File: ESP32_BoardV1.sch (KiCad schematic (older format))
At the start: 22 parts, among them J2 ISP, J3 To Sensor, J4 EXT. IO 1, J5 EXT. IO 1, Q1 UMH3N, U1 MIC5528-3.3YMT-TR, U2 ESP32-WROOM-32E(8MB)

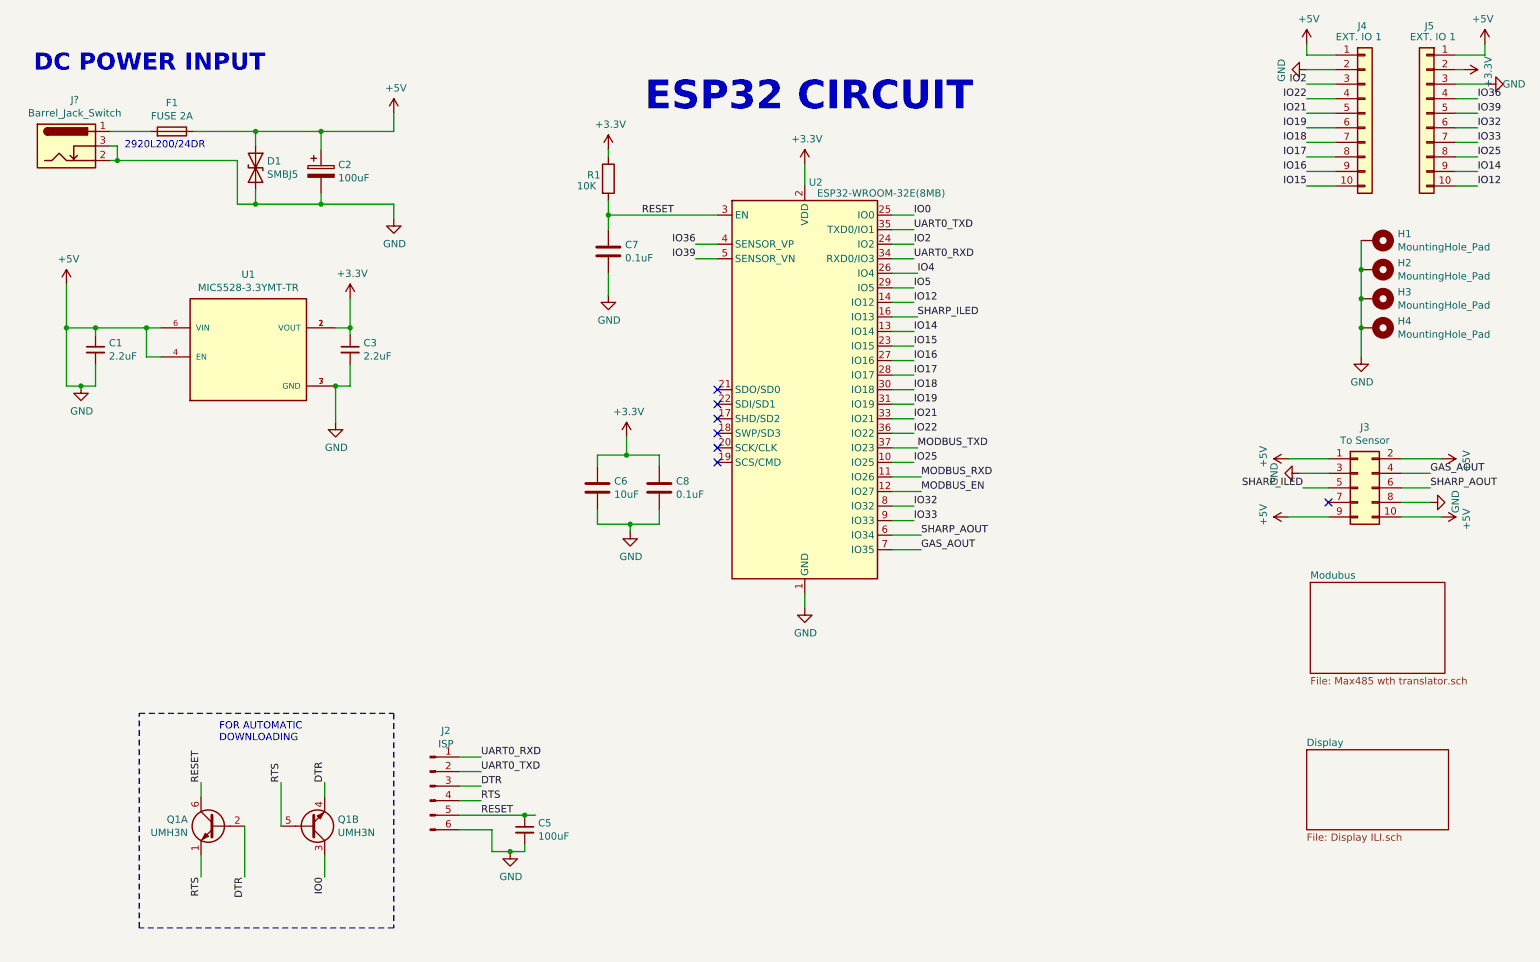
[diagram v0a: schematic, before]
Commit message: Recreated PCB file
Removed old PCB files, Schematic error in existing PCB has been rectfied
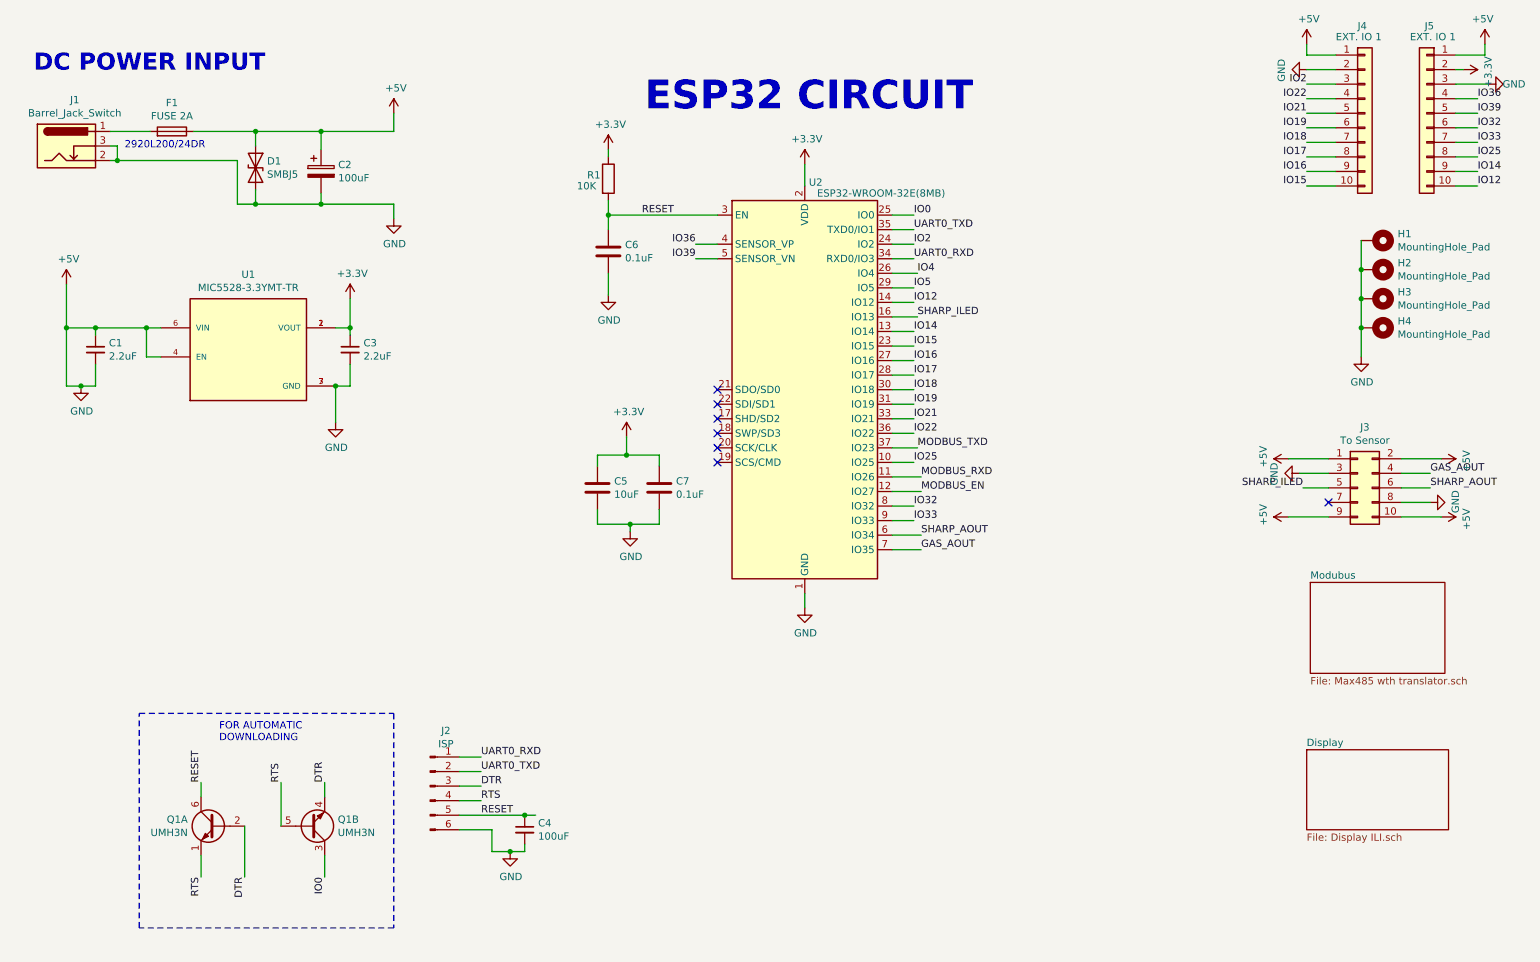
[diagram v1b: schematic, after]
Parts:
- J1: renamed from J?; footprint (none) -> Connector_BarrelJack:BarrelJack_Horizontal
- renumbered C5 to C4, C6 to C5, C7 to C6, C8 to C7
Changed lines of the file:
@@
 $Descr A4 11693 8268
 encoding utf-8
-Sheet 1 2
+Sheet 1 3
 Title ""
 Date "2020-10-15"
@@
 P 4875 2275
 AR Path="/5F7FDDC6/5F80494D" Ref="C?"  Part="1"
-AR Path="/5F80494D" Ref="C7"  Part="1"
-F 0 "C7" H 4990 2321 50  0000 L CNN
+AR Path="/5F80494D" Ref="C6"  Part="1"
+F 0 "C6" H 4990 2321 50  0000 L CNN
 F 1 "0.1uF" H 4990 2230 50  0000 L CNN
 F 2 "Capacitor_SMD:C_0805_2012Metric" H 4913 2125 50  0001 C CNN
@@
 P 5225 3900
 AR Path="/5F7FDDC6/5F80495A" Ref="C?"  Part="1"
-AR Path="/5F80495A" Ref="C8"  Part="1"
-F 0 "C8" H 5340 3946 50  0000 L CNN
+AR Path="/5F80495A" Ref="C7"  Part="1"
+F 0 "C7" H 5340 3946 50  0000 L CNN
 F 1 "0.1uF" H 5340 3855 50  0000 L CNN
 F 2 "Capacitor_SMD:C_0805_2012Metric" H 5263 3750 50  0001 C CNN
@@
 P 4800 3900
 AR Path="/5F7FDDC6/5F8049B7" Ref="C?"  Part="1"
-AR Path="/5F8049B7" Ref="C6"  Part="1"
-F 0 "C6" H 4915 3946 50  0000 L CNN
+AR Path="/5F8049B7" Ref="C5"  Part="1"
+F 0 "C5" H 4915 3946 50  0000 L CNN
 F 1 "10uF" H 4915 3855 50  0000 L CNN
 F 2 "Capacitor_SMD:C_0805_2012Metric" H 4838 3750 50  0001 C CNN
@@
 	3850 6150 4300 6150
 $Comp
-L Device:C_Small C5
+L Device:C_Small C4
 U 1 1 61CDDA04
 P 4300 6250
-F 0 "C5" H 4392 6296 50  0000 L CNN
+F 0 "C4" H 4392 6296 50  0000 L CNN
 F 1 "100uF" H 4392 6205 50  0000 L CNN
 F 2 "Capacitor_SMD:C_1206_3216Metric" H 4300 6250 50  0001 C CNN
@@
 	7000 2425 6825 2425
 $Comp
-L Connector:Barrel_Jack_Switch J?
+L Connector:Barrel_Jack_Switch J1
 U 1 1 61D95332
 P 1150 1550
-F 0 "J?" H 1207 1867 50  0000 C CNN
+F 0 "J1" H 1207 1867 50  0000 C CNN
 F 1 "Barrel_Jack_Switch" H 1207 1776 50  0000 C CNN
-F 2 "" H 1200 1510 50  0001 C CNN
+F 2 "Connector_BarrelJack:BarrelJack_Horizontal" H 1200 1510 50  0001 C CNN
 F 3 "~" H 1200 1510 50  0001 C CNN
 	1    1150 1550

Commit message: Pheripherial added 22.12.21
Added display connector, I2C connector, button and MAX3485
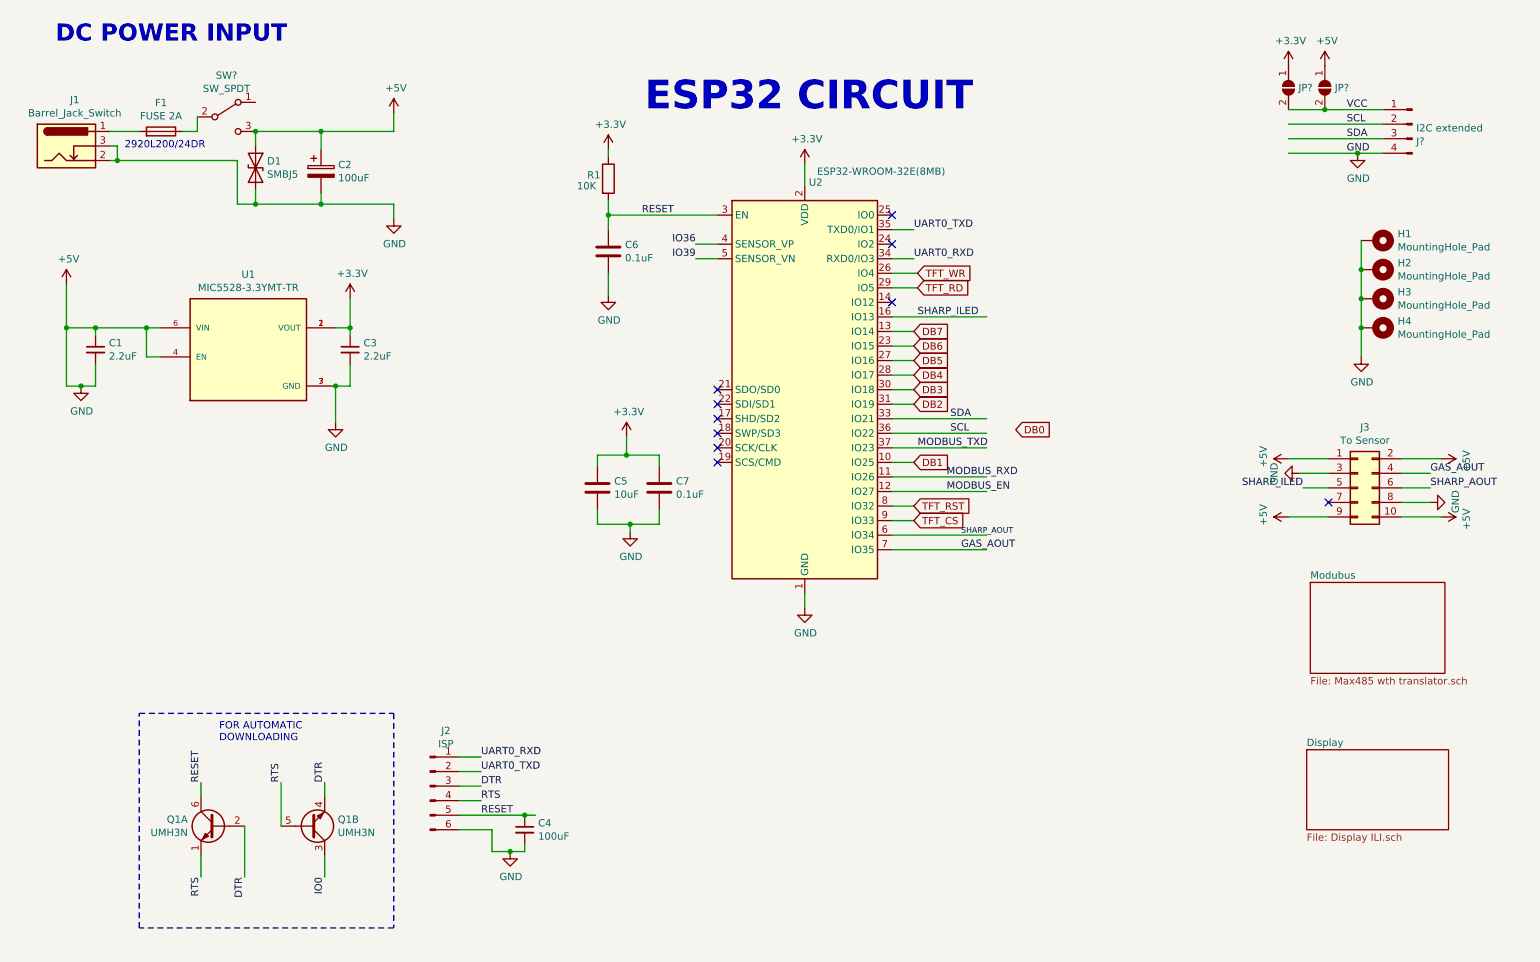
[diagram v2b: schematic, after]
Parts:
- removed J4, J5: EXT. IO 1, Connector_PinHeader_2.54mm:PinHeader_1x10_P2.54mm_Vertical, symbol Connector_Generic:Conn_01x10
- added J?: I2C extended, symbol Connector:Conn_01x04_Male
- added JP? (x2): SolderJumper_2_Open, Resistor_SMD:R_0805_2012Metric, symbol Jumper:SolderJumper_2_Open
- added SW?: SW_SPDT, symbol Switch:SW_SPDT
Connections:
- net labels added: DB0, DB1, DB2, DB3, DB4, DB5, DB6, DB7, SCL, SDA, TFT_CS, TFT_RD, TFT_RST, TFT_WR, VCC
- net labels removed: IO12, IO14, IO15, IO16, IO17, IO18, IO19, IO2, IO21, IO22, IO25, IO32, IO33, IO4, IO5
- wire segments 130 -> 112
- no-connect marks 7 -> 10
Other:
- moved on the sheet: F1

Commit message: 24.12.21
Board layout added, Step file added
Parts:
- removed C1, C3: 2.2uF, Capacitor_SMD:C_0603_1608Metric, symbol Device:C_Small
- removed C4: 100uF, Capacitor_SMD:C_1206_3216Metric, symbol Device:C_Small
- removed J3: To Sensor, Connector_IDC:IDC-Header_2x05_P2.54mm_Vertical, symbol Connector_Generic:Conn_02x05_Odd_Even
- removed U1: MIC5528-3.3YMT-TR, SnapEDA Library:SON40P120X120X60-7N, symbol MIC5528-3.3YMT-TR:MIC5528-3.3YMT-TR
- added C1: 10uF, Capacitor_SMD:CP_Elec_3x5.4, symbol Device:CP_Small
- added C10, C7: 0.1uF, Capacitor_SMD:C_0402_1005Metric_Pad0.74x0.62mm_HandSolder, symbol Device:C
- added C3: 22uF, Capacitor_SMD:CP_Elec_5x5.4, symbol Device:CP_Small
- added C9: 10uF, Capacitor_SMD:C_0402_1005Metric_Pad0.74x0.62mm_HandSolder, symbol Device:C
- added J3: GPIO expanded, SnapEDA Library:JST_SM04B-SRSS-TB(LF)(SN), symbol Connector:Conn_01x04_Male
- added J4: sensor, connector:JST_SM05B-SRSS-TB(LF)(SN), symbol Connector:Conn_01x05_Male
- added J7: Display, Connector_FFC-FPC:Hirose_FH12-40S-0.5SH_1x40-1MP_P0.50mm_Horizontal, symbol Connector:Conn_01x40_Female
- added R10, R2, R9: 10k, Resistor_SMD:R_0402_1005Metric_Pad0.72x0.64mm_HandSolder, symbol Device:R
- added U1: AZ1117-3.3, Package_TO_SOT_SMD:SOT-223-3_TabPin2, symbol Regulator_Linear:AZ1117-3.3
- C4: renamed from C5; footprint Capacitor_SMD:C_0805_2012Metric -> Capacitor_SMD:C_0402_1005Metric_Pad0.74x0.62mm_HandSolder
- C5: renamed from C6; footprint Capacitor_SMD:C_0805_2012Metric -> Capacitor_SMD:C_0402_1005Metric_Pad0.74x0.62mm_HandSolder
- C6: renamed from C7; footprint Capacitor_SMD:C_0805_2012Metric -> Capacitor_SMD:C_0402_1005Metric_Pad0.74x0.62mm_HandSolder
- H1, H2, H3, H4: footprint MountingHole:MountingHole_3.5mm_Pad_Via -> MountingHole:MountingHole_4.3mm_M4_Pad_Via
- J1: footprint Connector_BarrelJack:BarrelJack_Horizontal -> Connector_BarrelJack:BarrelJack_CLIFF_FC681465S_SMT_Horizontal
- J5: renamed from J?; footprint (none) -> SnapEDA Library:JST_SM04B-SRSS-TB(LF)(SN)
- JP1, JP2: renamed from JP?; footprint Resistor_SMD:R_0805_2012Metric -> Resistor_SMD:R_0402_1005Metric_Pad0.72x0.64mm_HandSolder
- R1: footprint Resistor_SMD:R_0805_2012Metric -> Resistor_SMD:R_0402_1005Metric_Pad0.72x0.64mm_HandSolder
- SW1: renamed from SW?; footprint (none) -> Button_Switch_THT:SW_Slide_1P2T_CK_OS102011MS2Q
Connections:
- net labels added: CTP_INT, CTP_SCL, CTP_SDA, GPIO15, GPIO16, GPIO17, GPIO32, GPIO33, TFT_AO, TFT_SCLK, TFT_SDI
- net labels removed: DB0, DB1, DB2, DB3, DB4, DB5, DB6, DB7, TFT_RD, TFT_WR
- wire segments 112 -> 197
- no-connect marks 10 -> 8
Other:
- moved on the sheet: C2, C4, C5, C6, D1, F1, J1, J2, J5, JP1, JP2, Q1A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
